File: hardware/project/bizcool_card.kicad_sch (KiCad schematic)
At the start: 145 parts, among them J1 XL-1005SURC, J2 Conn_01x03, SW1 SW_Push, SW2 SW_Push, U1 PRTR5V0U2X, U2 ME6211C33M5G, U3 ESP32-C3FN4, U4 W25Q128JVS

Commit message: fix: correct LDO component part name
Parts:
- U2: value ME6211C33M5G -> AMS1117-3.3
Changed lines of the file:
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@@
       (effects (font (size 1.27 1.27)))
     )
-    (property "Value" "ME6211C33M5G" (at 88.9 10.16 0)
+    (property "Value" "AMS1117-3.3" (at 88.9 10.16 0)
       (effects (font (size 1.27 1.27)) hide)
     )

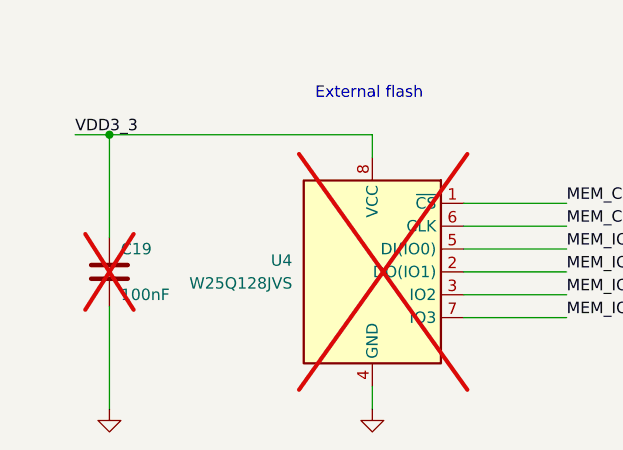
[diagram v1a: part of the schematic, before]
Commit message: fix: LCSC component references
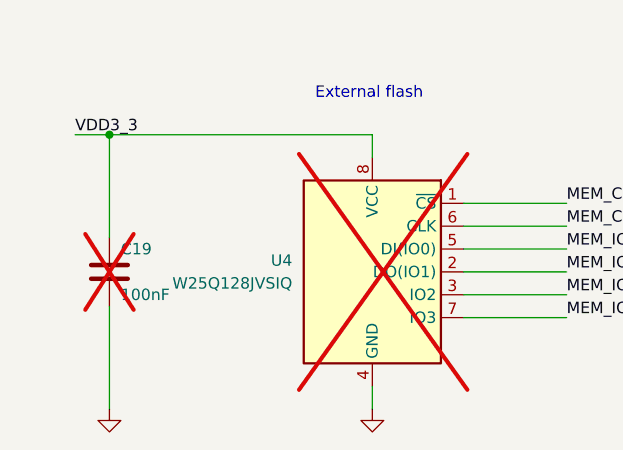
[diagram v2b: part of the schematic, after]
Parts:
- C16: LCSC Part (none) -> C60133
- R20, R21, R5, R8: LCSC Part C965790 -> C60490
- U3: LCSC Part (none) -> C5143572
- U4: value W25Q128JVS -> W25Q128JVSIQ; LCSC Part (none) -> C97521
- XTAL1: LCSC Part (none) -> C7294598
- XTAL2: LCSC Part (none) -> C7294751; Part CF4040M00010001 -> DF2032K76812001
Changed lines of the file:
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@@
       (effects (font (size 1.27 1.27)) (justify left))
     )
-    (property "Value" "W25Q128JVS" (at 44.45 172.72 0)
+    (property "Value" "W25Q128JVSIQ" (at 44.45 172.72 0)
       (effects (font (size 1.27 1.27)) (justify left))
     )
@@
       (effects (font (size 1.27 1.27)) hide)
     )
+    (property "LCSC Part" "C97521" (at 53.34 171.45 0)
+      (effects (font (size 1.27 1.27)) hide)
+    )
     (pin "2")
     (pin "6")
@@
       (effects (font (size 1.27 1.27)) hide)
     )
+    (property "LCSC Part" "C60133" (at 233.68 148.59 0)
+      (effects (font (size 1.27 1.27)) hide)
+    )
     (pin "2")
     (pin "1")
@@
       (effects (font (size 1.27 1.27)) hide)
     )
-    (property "Datasheet" "~" (at 31.75 87.63 0)
+    (property "Datasheet" "https://datasheet.lcsc.com/lcsc/2306211559_huaxindianzi-CF4040M00010001_C7294598.pdf" (at 31.75 87.63 0)
       (effects (font (size 1.27 1.27)) hide)
     )
@@
       (effects (font (size 1.27 1.27)) hide)
     )
+    (property "LCSC Part" "C7294598" (at 31.75 87.63 0)
+      (effects (font (size 1.27 1.27)) hide)
+    )
     (pin "3")
     (pin "1")
@@
       (effects (font (size 1.27 1.27)) hide)
     )
+    (property "LCSC Part" "C5143572" (at 139.7 147.32 0)
+      (effects (font (size 1.27 1.27)) hide)
+    )
     (pin "29")
     (pin "17")
@@
       (effects (font (size 1.27 1.27)) hide)
     )
-    (property "LCSC Part" "C965790" (at 233.68 139.7 0)
+    (property "LCSC Part" "C60490" (at 233.68 139.7 0)
       (effects (font (size 1.27 1.27)) hide)
     )
@@
       (effects (font (size 1.27 1.27)) hide)
     )
-    (property "LCSC Part" "C965790" (at 201.93 139.7 0)
+    (property "LCSC Part" "C60490" (at 201.93 139.7 0)
       (effects (font (size 1.27 1.27)) hide)
     )
@@
       (effects (font (size 1.27 1.27)) hide)
     )
-    (property "LCSC Part" "C965790" (at 175.26 138.43 0)
+    (property "LCSC Part" "C60490" (at 175.26 138.43 0)
       (effects (font (size 1.27 1.27)) hide)
     )
@@
       (effects (font (size 1.27 1.27)) hide)
     )
-    (property "LCSC Part" "C965790" (at 168.91 138.43 0)
+    (property "LCSC Part" "C60490" (at 168.91 138.43 0)
       (effects (font (size 1.27 1.27)) hide)
     )
@@
       (effects (font (size 1.27 1.27)) hide)
     )
-    (property "Datasheet" "~" (at 31.75 119.38 0)
+    (property "Datasheet" "https://datasheet.lcsc.com/lcsc/2306211602_huaxindianzi-DF2032K76812001_C7294751.pdf" (at 31.75 119.38 0)
+      (effects (font (size 1.27 1.27)) hide)
+    )
+    (property "Part" "DF2032K76812001" (at 31.75 119.38 0)
       (effects (font (size 1.27 1.27)) hide)
     )
-    (property "Part" "CF4040M00010001" (at 31.75 119.38 0)
+    (property "LCSC Part" "C7294751" (at 31.75 119.38 0)
       (effects (font (size 1.27 1.27)) hide)
     )

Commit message: fix disconnected cut outline, change push button footprints
- Edge.Cuts layer was not a properly closed shape
- adopted quite bulky 6x6 SMT push buttons (still DNP though)
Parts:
- J2: now left out of the parts list
- SW1, SW2: footprint Button_Switch_SMD:SW_Push_1P1T_NO_Vertical_Wuerth_434133025816 -> Button_Switch_SMD:SW_Push_1P1T_NO_6x6mm_H9.5mm
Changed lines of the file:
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@@
   )
   (symbol (lib_id "Connector_Generic:Conn_01x06") (at 256.54 110.49 0) (unit 1)
-    (in_bom yes) (on_board yes) (dnp yes)
+    (in_bom no) (on_board yes) (dnp yes)
     (property "Reference" "J2" (at 255.27 105.41 0)
       (effects (font (size 1.27 1.27)) (justify left))
@@
       (effects (font (size 1.27 1.27)) (justify right) hide)
     )
-    (property "Footprint" "Button_Switch_SMD:SW_Push_1P1T_NO_Vertical_Wuerth_434133025816" (at 190.5 149.86 0)
+    (property "Footprint" "Button_Switch_SMD:SW_Push_1P1T_NO_6x6mm_H9.5mm" (at 190.5 149.86 0)
       (effects (font (size 1.27 1.27)) hide)
     )
@@
       (effects (font (size 1.27 1.27)) (justify right) hide)
     )
-    (property "Footprint" "Button_Switch_SMD:SW_Push_1P1T_NO_Vertical_Wuerth_434133025816" (at 222.25 149.86 0)
-      (effects (font (size 1.27 1.27)) hide)
-    )
+    (property "Footprint" "Button_Switch_SMD:SW_Push_1P1T_NO_6x6mm_H9.5mm" (at 222.25 149.86 0)
+      (effects (font (size 1.27 1.27)) hide)
+    )

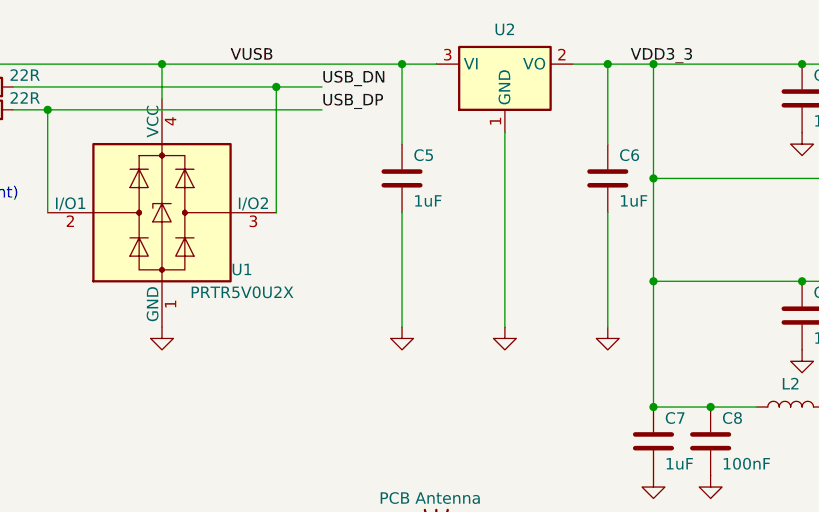
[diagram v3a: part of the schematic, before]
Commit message: change LDO regulator
switched to a SOT-23-3 LDO reg, a smaller one (400mA).
technically not in-spec, should use 2 of these.
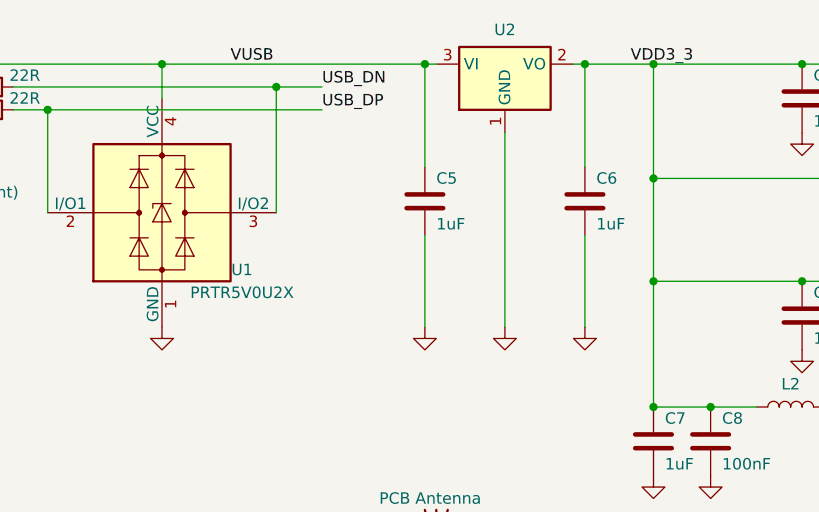
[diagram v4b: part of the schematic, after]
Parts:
- U2: value AMS1117-3.3 -> H7233-1; footprint Package_TO_SOT_SMD:SOT-223-3_TabPin2 -> Package_TO_SOT_SMD:SOT-23-3; LCSC Part C347256 -> C277859
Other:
- moved on the sheet: C5, C6

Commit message: fix: d1-d6 reordering, re-routing
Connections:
- net at D10.1 (K), D15.2 (A), D16.1 (K)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: now also D1.1 (K), D2.2 (A), D5.2 (A), D6.1 (K); no longer D1.2 (A), D2.1 (K), D5.1 (K), D6.2 (A)
- net at D11.2 (A), D12.1 (K), D17.2 (A)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: now also D3.1 (K), D4.2 (A), D5.1 (K), D6.2 (A); no longer D3.2 (A), D4.1 (K), D5.2 (A), D6.1 (K)
- net at D13.2 (A), D14.1 (K), D21.2 (A)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: now also D1.2 (A), D2.1 (K), D3.2 (A), D4.1 (K); no longer D1.1 (K), D2.2 (A), D3.1 (K), D4.2 (A)
